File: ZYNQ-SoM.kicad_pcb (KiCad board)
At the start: 6 copper layers, 50 x 40 mm, 173 parts, among them IC501 TPS51206DSQR, J401 AXK500137YG, J402 AXK500137YG, Q201 MMBT3904, U201 xc7z010clg400, U202 W25Q256FVEI, U301 MT41K256M16TW-107_P, U501 TPS62130ARGTR, U502 TPS62130ARGTR, U503 SPX3819M5-L-3-3, U504 TPS62130ARGTR, U701 33.3333MHz

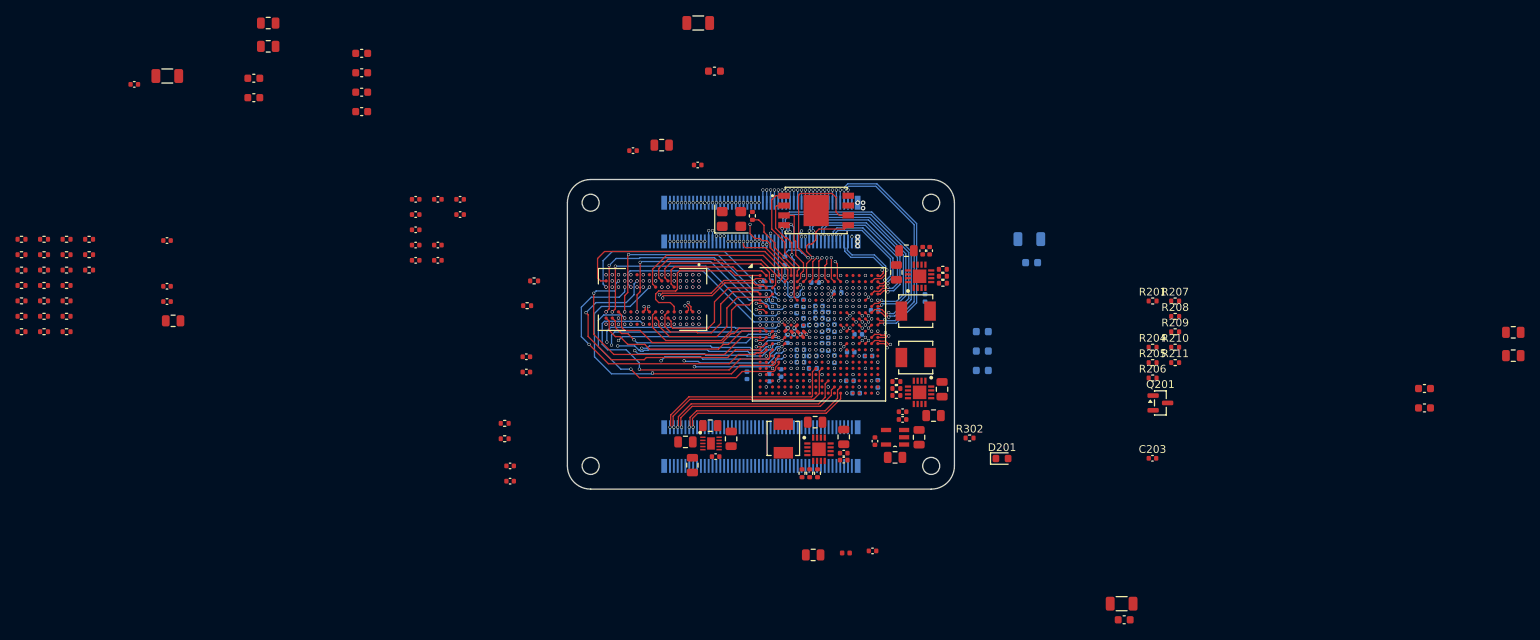
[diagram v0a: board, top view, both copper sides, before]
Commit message: layout: routing bank 34
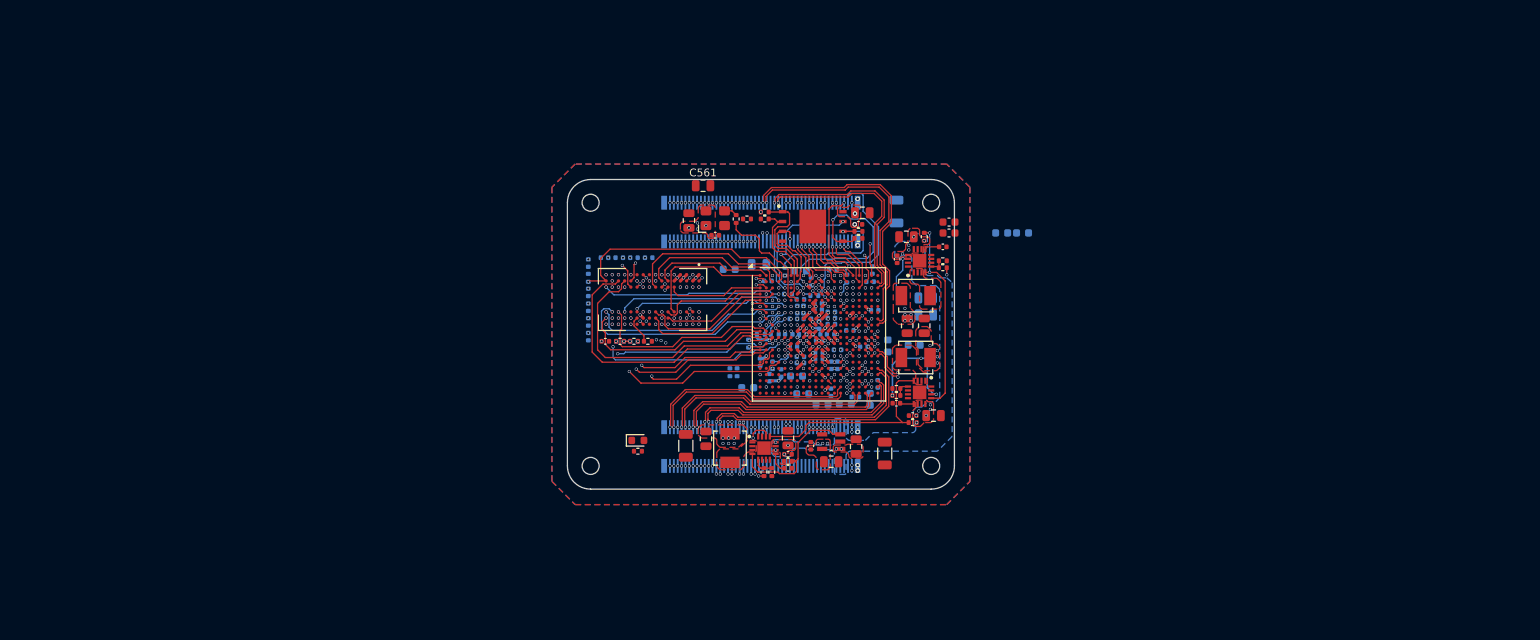
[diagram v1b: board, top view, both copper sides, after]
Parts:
- removed C315, C513, C515, C529, C531: 10u, Capacitor_SMD:C_0805_2012Metric
- removed C317, C321, C322: 100n, Capacitor_SMD:C_0402_1005Metric
- removed C518: 100u, Capacitor_SMD:C_1206_3216Metric
- removed C520, C535: 470n, Capacitor_SMD:C_0402_1005Metric
- removed IC501: TPS51206DSQR, Project:SON40P200X200X80-11N
- removed Q201: MMBT3904, Package_TO_SOT_SMD:SOT-23
- removed R204: 330R, Resistor_SMD:R_0402_1005Metric
- removed R308, R309, R310, R311, R312, R313, R314, R315, R316, R317, R318, R319, R320, R321, R322, R323, R324, R325, R326, R327, R328, R329, R330: 40R2, Resistor_SMD:R_0402_1005Metric
- added R303: 80R6, Resistor_SMD:R_0402_1005Metric, F.Cu at (108.6, 80.9)
- added R706: 10k, Resistor_SMD:R_0402_1005Metric, B.Cu at (131.5, 73.2)
- C301, C302, C303, C304, C305, C306, C308, C309, C310, C312, C313, C314, C507, C508, C521, C523, C533, C537, C546, C548, C550, C553, C557, C567, C702, FB501, R207, R211, R302, R304, R305, R306: moved to B.Cu
- C311: value 10n -> 100n; moved to B.Cu
- R201: value 1k -> 330R
- R206: value 470R -> 4k7
- R307: value 40R2 -> 80R6
- U202: footprint Project:IC_W25N04KVZEIU -> Project:SON127P800X600X80-9N-D
- moved C561 106.9 mm to (117.5, 60.8)
- moved C521 92.9 mm to (146.3, 77.5), turned to 180 degrees
- moved C525 91.7 mm to (149.3, 65.5)
- moved C567 91.6 mm to (120.9, 71.6)
- moved C527 91.5 mm to (149.3, 66.9)
- moved C523 91.0 mm to (146.3, 75.3), turned to 180 degrees
- moved C553 87.3 mm to (158.8, 66.9)
- moved C540 85.5 mm to (138.1, 64.3)
- moved C557 84.1 mm to (156.1, 66.9), turned to 180 degrees
- moved C546 82.0 mm to (130.1, 71.8)
- moved R307 78.4 mm to (106.8, 80.9)
- moved C537 75.7 mm to (135.9, 89.0), turned to 180 degrees
- moved C533 74.8 mm to (132.9, 89.1), turned to 180 degrees
- moved R205 67.5 mm to (109.1, 95.1)
- moved R209 55.0 mm to (125.5, 65.1)
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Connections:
- net Net-(U501-SW_1) renamed /POWER/1V0_SW
- net Net-(U502-SW_1) renamed /POWER/1V5_SW
- net Net-(U504-SW_1) renamed /POWER/1V8_SW
- C311 pad 1: VTTREF -> +VTTREF
- C313 pad 1: VTTREF -> +VTTREF
- C561 pad 1: +1V8 -> +3V3
- C567 pad 1: +1V8 -> +3V3
- C573 pad 1: +1V8 -> +3V3
- D201 pad 2: DONE -> +3V3
- J401 pad 100: unconnected-(J401-Pad100) -> GND
- J401 pad 15: unconnected-(J401-Pad15) -> GND
- J401 pad 16: unconnected-(J401-Pad16) -> GND
- J401 pad 18: unconnected-(J401-Pad18) -> PL_B34_IO22_P
- J401 pad 20: unconnected-(J401-Pad20) -> PL_B34_IO22_N
- J401 pad 21: unconnected-(J401-Pad21) -> GND
- J401 pad 22: unconnected-(J401-Pad22) -> GND
- J401 pad 24: unconnected-(J401-Pad24) -> PL_B34_IO12_N
- J401 pad 26: unconnected-(J401-Pad26) -> PL_B34_IO12_P
- J401 pad 27: unconnected-(J401-Pad27) -> GND
- J401 pad 28: unconnected-(J401-Pad28) -> GND
- J401 pad 30: unconnected-(J401-Pad30) -> PL_B34_IO20_P
- J401 pad 32: unconnected-(J401-Pad32) -> PL_B34_IO20_N
- J401 pad 33: unconnected-(J401-Pad33) -> GND
- J401 pad 34: unconnected-(J401-Pad34) -> GND
- J401 pad 36: unconnected-(J401-Pad36) -> PL_B34_IO13_N
- J401 pad 38: unconnected-(J401-Pad38) -> PL_B34_IO13_P
- J401 pad 39: unconnected-(J401-Pad39) -> GND
- J401 pad 40: unconnected-(J401-Pad40) -> GND
- J401 pad 42: unconnected-(J401-Pad42) -> PL_B34_IO21_N
- J401 pad 44: unconnected-(J401-Pad44) -> PL_B34_IO21_P
- J401 pad 45: unconnected-(J401-Pad45) -> GND
- J401 pad 46: unconnected-(J401-Pad46) -> GND
- J401 pad 48: unconnected-(J401-Pad48) -> PL_B34_IO24_N
- J401 pad 50: unconnected-(J401-Pad50) -> PL_B34_IO24_P
- J401 pad 51: unconnected-(J401-Pad51) -> GND
- J401 pad 52: unconnected-(J401-Pad52) -> GND
- J401 pad 54: unconnected-(J401-Pad54) -> PL_B34_IO18_P
- J401 pad 56: unconnected-(J401-Pad56) -> PL_B34_IO18_N
- J401 pad 57: unconnected-(J401-Pad57) -> GND
- J401 pad 58: unconnected-(J401-Pad58) -> GND
- J401 pad 60: unconnected-(J401-Pad60) -> PL_B34_IO10_N
- J401 pad 62: unconnected-(J401-Pad62) -> PL_B34_IO10_P
- J401 pad 63: unconnected-(J401-Pad63) -> GND
- J401 pad 64: unconnected-(J401-Pad64) -> GND
- J401 pad 66: unconnected-(J401-Pad66) -> PL_B34_IO5_N
- J401 pad 68: unconnected-(J401-Pad68) -> PL_B34_IO5_P
- J401 pad 69: unconnected-(J401-Pad69) -> GND
- J401 pad 70: unconnected-(J401-Pad70) -> GND
- J401 pad 72: unconnected-(J401-Pad72) -> PL_B34_IO15_P
- J401 pad 74: unconnected-(J401-Pad74) -> PL_B34_IO15_N
- J401 pad 75: unconnected-(J401-Pad75) -> GND
- J401 pad 76: unconnected-(J401-Pad76) -> GND
- J401 pad 78: unconnected-(J401-Pad78) -> PL_B34_IO16_P
- J401 pad 80: unconnected-(J401-Pad80) -> PL_B34_IO16_N
- J401 pad 81: unconnected-(J401-Pad81) -> GND
- J401 pad 82: unconnected-(J401-Pad82) -> GND
- J401 pad 84: unconnected-(J401-Pad84) -> PL_B34_IO17_N
- J401 pad 86: PL_B34_IO8_N -> PL_B34_IO17_P
- J401 pad 87: unconnected-(J401-Pad87) -> GND
- J401 pad 88: PL_B34_IO8_P -> GND
- J401 pad 90: unconnected-(J401-Pad90) -> PL_B34_IO7_N
- J401 pad 92: PL_B34_IO4_N -> PL_B34_IO7_P
- J401 pad 93: unconnected-(J401-Pad93) -> GND
- J401 pad 94: PL_B34_IO4_P -> GND
- J401 pad 96: PL_B34_IO1_P -> PL_B34_IO8_N
- J401 pad 98: PL_B34_IO1_N -> PL_B34_IO8_P
- J401 pad 99: unconnected-(J401-Pad99) -> GND
- J402 pad 11: PL_B35_IO1_N -> PS_MIO20
- J402 pad 12: PL_B35_IO22_P -> DONE
- J402 pad 13: PL_B35_IO1_P -> PS_MIO22
- J402 pad 14: PL_B35_IO22_N -> PS_POR_B
- J402 pad 17: PL_B35_IO4_P -> PS_MIO24
- J402 pad 18: PL_B35_IO20_P -> PS_MIO19
- J402 pad 19: PL_B35_IO4_N -> PS_MIO26
- J402 pad 20: PL_B35_IO20_N -> PS_MIO25
- J402 pad 23: PL_B35_IO15_P -> SD_DATA3
- J402 pad 24: PL_B35_IO13_P -> PS_MIO17
- J402 pad 25: PL_B35_IO15_N -> I2C0_SCL
- J402 pad 26: PL_B35_IO13_N -> PS_MIO21
- J402 pad 29: PL_B35_IO19_P -> I2C0_SDA
- J402 pad 30: PL_B35_IO14_P -> PS_MIO23
- J402 pad 31: PL_B35_IO19_N -> SD_DATA1
- J402 pad 32: PL_B35_IO14_N -> PS_MIO27
- J402 pad 35: PL_B35_IO18_P -> QSPI_D2_PS_MIO4
- J402 pad 36: PL_B35_IO16_N -> PS_MIO49
- J402 pad 37: PL_B35_IO18_N -> QSPI_D3_PS_MIO5
- J402 pad 38: PL_B35_IO16_P -> PS_MIO47
- J402 pad 42: PL_B35_IO5_N -> PL_B35_IO1_N
- J402 pad 44: PL_B35_IO5_P -> PL_B35_IO1_P
- J402 pad 47: PS_MIO47 -> PS_MIO16
- J402 pad 48: PL_B35_IO23_N -> PL_B35_IO17_N
- J402 pad 49: PS_MIO48 -> PS_MIO18
- J402 pad 5: PL_B35_IO2_P -> SD_DATA2
- J402 pad 50: PL_B35_IO23_P -> PL_B35_IO17_P
- J402 pad 53: I2C0_SDA -> PS_MIO53
- J402 pad 54: PL_B35_IO7_N -> PL_B35_IO9_N
- J402 pad 55: I2C0_SCL -> PS_MIO48
- J402 pad 56: PL_B35_IO7_P -> PL_B35_IO9_P
- J402 pad 59: PS_MIO9 -> PS_MIO52
- J402 pad 6: PL_B35_IO17_N -> SD_DATA0
- J402 pad 60: PL_B35_IO8_P -> PL_B35_IO7_N
- J402 pad 61: SD_DATA1 -> OTG_NXT
- J402 pad 62: PL_B35_IO8_N -> PL_B35_IO7_P
- J402 pad 65: SD_DATA3 -> OTG_DATA4
- J402 pad 66: PL_B35_IO9_N -> PL_B35_IO11_N
- J402 pad 67: SD_CMD -> OTG_DATA2
- J402 pad 68: PL_B35_IO9_P -> PL_B35_IO11_P
- J402 pad 7: PL_B35_IO2_N -> SD_CMD
- J402 pad 71: SD_CLK -> OTG_DATA7
- J402 pad 72: PL_B35_IO10_P -> PL_B35_IO14_P
- J402 pad 73: SD_DATA0 -> OTG_nRST
- J402 pad 74: PL_B35_IO10_N -> PL_B35_IO14_N
- J402 pad 77: SD_DATA2 -> OTG_DATA0
- J402 pad 78: PL_B35_IO3_N -> PL_B35_IO12_N
- J402 pad 79: OTG_DATA0 -> OTG_STP
- J402 pad 8: PL_B35_IO17_P -> SD_CLK
- J402 pad 80: PL_B35_IO3_P -> PL_B35_IO12_P
- J402 pad 83: OTG_DATA6 -> OTG_DATA1
- J402 pad 84: OTG_DATA7 -> PL_B35_IO13_N
- J402 pad 86: OTG_nRST -> PL_B35_IO13_P
- J402 pad 89: OTG_DATA2 -> OTG_DATA6
- J402 pad 90: OTG_NXT -> TCK
- J402 pad 91: OTG_DATA5 -> OTG_CLK
- J402 pad 92: OTG_DATA4 -> TMS
- J402 pad 95: OTG_CLK -> OTG_DATA5
- J402 pad 96: OTG_STP -> TDO
- J402 pad 98: OTG_DATA1 -> TDI
- R201 pad 1: +1V5 -> +3V3
- R201 pad 2: Net-(Q201-B) -> DONE
- R205 pad 2: Net-(Q201-C) -> GND
- R207 pad 1: +3V3 -> GND
- R307 pad 1: /DDR3/DDR_A0 -> +1V5
- R307 pad 2: +DDRVTT -> +VTTREF
- U201 pad A13: Net-(U201F-VCCO_MIO1_501[4]-PadA13) -> +3V3
- U201 pad B16: Net-(U201F-VCCO_MIO1_501[4]-PadA13) -> +3V3
- U201 pad C6: PS_MIO11 -> unconnected-(U201E-PS_MIO11_500-PadC6)
- U201 pad D12: Net-(U201F-VCCO_MIO1_501[4]-PadA13) -> +3V3
- U201 pad D9: PS_MIO12 -> unconnected-(U201E-PS_MIO12_500-PadD9)
- U201 pad E11: PS_MIO_VREF -> unconnected-(U201F-PS_MIO_VREF_501-PadE11)
- U201 pad E15: Net-(U201F-VCCO_MIO1_501[4]-PadA13) -> +3V3
- U201 pad E6: PS_MIO0 -> unconnected-(U201E-PS_MIO0_500-PadE6)
- U201 pad E9: PS_MIO10 -> unconnected-(U201E-PS_MIO10_500-PadE9)
- U201 pad H6: VTTREF -> +VTTREF
- U201 pad L2: /DDR3/DDR_CLK_N -> /DDR3/DDR_CLK_P
- U201 pad M2: /DDR3/DDR_CLK_P -> /DDR3/DDR_CLK_N
- U201 pad P6: VTTREF -> +VTTREF
- U301 pad A3: /DDR3/DDR_D10 -> /DDR3/DDR_D8
- U301 pad A7: /DDR3/DDR_D14 -> /DDR3/DDR_D13
- U301 pad B8: /DDR3/DDR_D13 -> /DDR3/DDR_D14
- U301 pad C2: /DDR3/DDR_D8 -> /DDR3/DDR_D11
- U301 pad C3: /DDR3/DDR_D12 -> /DDR3/DDR_D10
- U301 pad D7: /DDR3/DDR_D11 -> /DDR3/DDR_D12
- U301 pad E3: /DDR3/DDR_D2 -> /DDR3/DDR_D6
- U301 pad F2: /DDR3/DDR_D1 -> /DDR3/DDR_D2
- U301 pad F7: /DDR3/DDR_D5 -> /DDR3/DDR_D0
- U301 pad F8: /DDR3/DDR_D6 -> /DDR3/DDR_D5
- U301 pad G2: /DDR3/DDR_D0 -> /DDR3/DDR_D1
- U301 pad H7: /DDR3/DDR_D7 -> /DDR3/DDR_D4
- U301 pad H8: /DDR3/DDR_D4 -> /DDR3/DDR_D7
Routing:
- net PL_B35_IO23_N: track 54.1 -> 0.00 mm, vias 2 -> 0
- net PL_B35_IO23_P: track 53.2 -> 0.00 mm, vias 2 -> 0
- net PL_B35_IO22_P: track 45.5 -> 0.00 mm, vias 2 -> 0
- net PL_B35_IO8_P: track 45.4 -> 0.00 mm, vias 2 -> 0
- net +VTTREF: track 0.00 -> 45.0 mm, vias 2 -> 6
- net PL_B35_IO22_N: track 44.4 -> 0.00 mm, vias 2 -> 0
- net PL_B35_IO8_N: track 44.3 -> 0.00 mm, vias 2 -> 0
- net PL_B35_IO20_P: track 43.8 -> 0.00 mm, vias 2 -> 0
- net PL_B35_IO20_N: track 43.6 -> 0.00 mm, vias 2 -> 0
- net PL_B35_IO11_P: track 0.00 -> 42.5 mm, vias 0 -> 2
- net PL_B35_IO11_N: track 0.00 -> 42.5 mm, vias 0 -> 2
- net PL_B35_IO10_N: track 41.2 -> 0.00 mm, vias 2 -> 0
- net PL_B35_IO10_P: track 40.9 -> 0.00 mm, vias 2 -> 0
- net PL_B35_IO12_P: track 0.00 -> 38.7 mm, vias 0 -> 2
- net PL_B35_IO12_N: track 0.00 -> 38.7 mm, vias 0 -> 2
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- added copper zone on F.Cu, net +1V0
- added copper zone on In4.Cu, net +1V0
- added copper zone on F.Cu, net +1V5
- added copper zone on In4.Cu, net +1V5
- added copper zone on F.Cu, net +1V8
- added copper zone on In4.Cu, net +1V8
- added copper zone on F.Cu, net +3V3
- added copper zone on In4.Cu, net +3V3
- added copper zone on B.Cu, net +5V
- added copper zone on F.Cu, net +5V
- added copper zone on In3.Cu, net +VCCIO_34
- added copper zone on In4.Cu, net +VCCIO_34
- added copper zone on In4.Cu, net +VCCIO_35
- added copper zone on F.Cu, net /POWER/1V0_SW
- added copper zone on F.Cu, net /POWER/1V5_SW
- added copper zone on F.Cu, net /POWER/1V8_SW
- added copper zone on B.Cu, net GND
- added copper zone on F.Cu, net GND
- added copper zone on In1.Cu, net GND
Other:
- board text added: "+1V5 DDR"
- board text added: "+3V3 BANK13"
- board text added: "+3V3 MIO"
- board text added: "+VCCIO 34"
- board text added: "+VCCIO 35"
- board text added: "1V0 / 1V8 MIXED VIAS FIRST"

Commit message: layout: finish basic bank34 routing
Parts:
- moved C562 4.08 mm to (126.3, 87.8)
- moved C547 0.50 mm to (134.9, 81.5)
- moved C554 0.29 mm to (134.0, 87.2)
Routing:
- net PL_B34_IO24_N: track 21.0 -> 0.69 mm
- net PL_B34_IO24_P: track 20.1 -> 0.13 mm
- net PL_B34_IO19_P: track 0.00 -> 15.2 mm, vias 0 -> 1
- net PL_B34_IO19_N: track 0.00 -> 14.8 mm, vias 0 -> 1
- net PL_B34_IO25: track 0.00 -> 9.06 mm, vias 0 -> 1
- net PL_B34_IO23_N: track 0.00 -> 8.63 mm, vias 0 -> 1
- net PL_B34_IO0: track 0.00 -> 7.80 mm, vias 0 -> 1
- net PL_B34_IO9_P: track 0.00 -> 6.77 mm
- net PL_B34_IO11_N: track 0.00 -> 6.42 mm
- net PL_B34_IO2_P: track 0.00 -> 6.38 mm, vias 0 -> 1
- net PL_B34_IO9_N: track 0.57 -> 6.77 mm
- net PL_B34_IO11_P: track 0.57 -> 6.09 mm
- net PL_B34_IO2_N: track 0.00 -> 5.45 mm, vias 0 -> 1
- net PL_B34_IO3_P: track 0.00 -> 5.36 mm
- net PL_B34_IO1_P: track 0.57 -> 5.90 mm
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- added copper zone on In3.Cu, net +1V0
- added copper zone on In3.Cu, net +1V8
- added copper zone on In3.Cu, net +3V3
- removed copper zone on In3.Cu, net +VCCIO_34

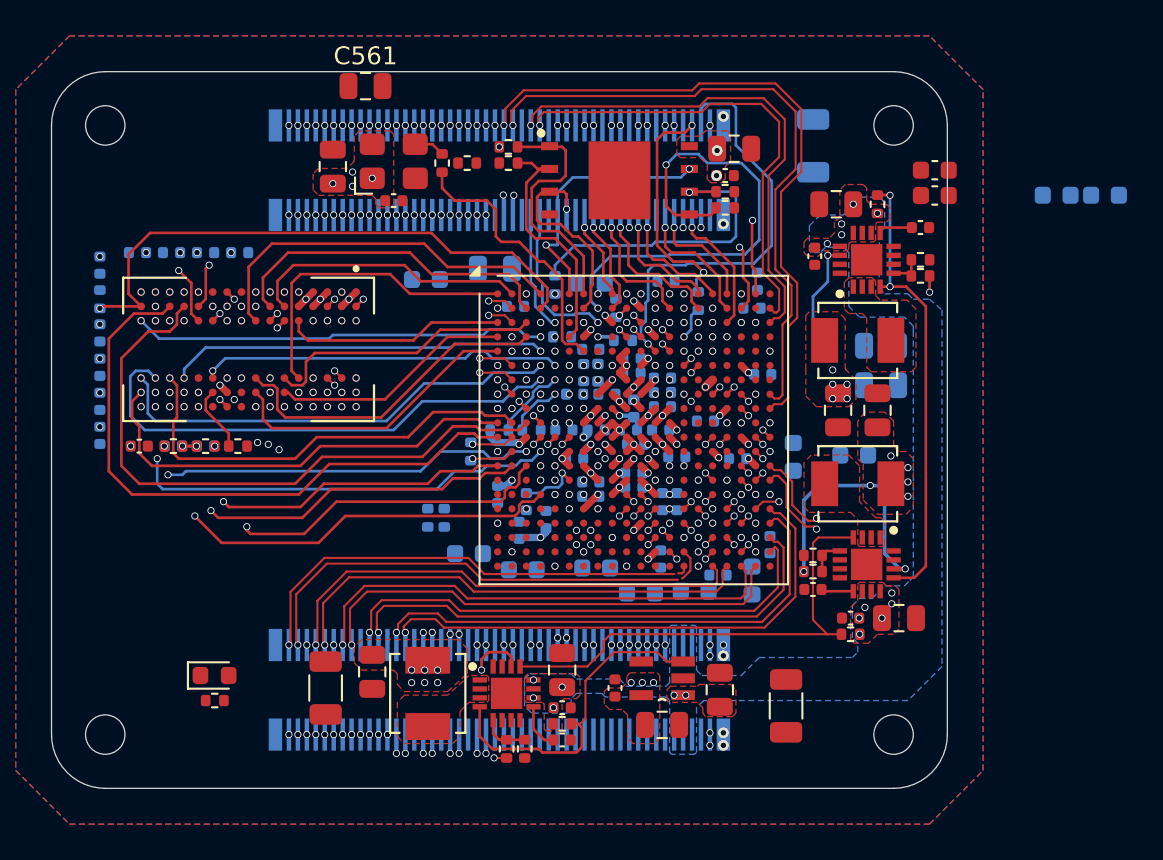
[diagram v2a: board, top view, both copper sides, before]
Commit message: layout: before rerouting ddr
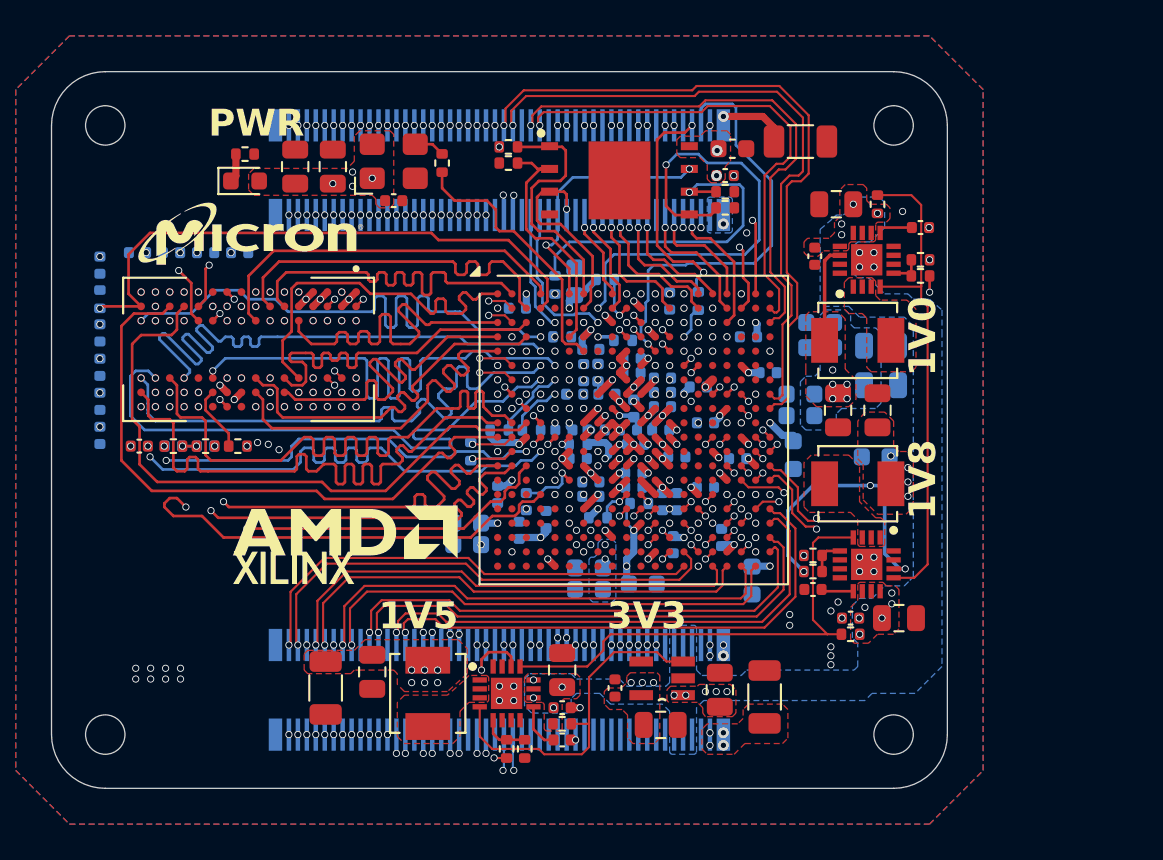
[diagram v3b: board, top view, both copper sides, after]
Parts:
- removed C537, C557: 4u7, Capacitor_SMD:C_0603_1608Metric
- C507, C540: footprint Capacitor_SMD:C_0805_2012Metric -> Capacitor_SMD:C_0603_1608Metric
- C525, C527, R201: moved to B.Cu
- C544: moved to F.Cu
- moved R205 30.5 mm to (110.8, 64.6)
- moved D201 27.7 mm to (110.8, 66.1)
- moved R201 21.3 mm to (132.8, 84.1)
- moved C567 20.9 mm to (133.0, 88.6)
- moved C553 17.4 mm to (142.9, 74.0), turned to 180 degrees
- moved C533 17.0 mm to (142.9, 75.4)
- moved C507 15.5 mm to (123.2, 86.4)
- moved C525 14.6 mm to (141.8, 78.0), turned to 180 degrees
- moved C527 14.4 mm to (141.8, 79.2), turned to 180 degrees
- moved R203 9.35 mm to (129.4, 80.8), turned to 180 degrees
- moved R202 8.58 mm to (130.5, 84.9), turned to 0 degrees
- moved C565 6.76 mm to (136.1, 77.6), turned to 0 degrees
- moved C561 5.97 mm to (113.6, 65.3), turned to 90 degrees
- moved C554 4.72 mm to (136.5, 83.2), turned to 0 degrees
- moved C562 3.86 mm to (130.0, 88.9)
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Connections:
- J401 pad 36: PL_B34_IO13_N -> PL_B34_IO13_P
- J401 pad 38: PL_B34_IO13_P -> PL_B34_IO13_N
- J401 pad 47: unconnected-(J401-Pad47) -> PL_B34_IO23_N
- J401 pad 48: PL_B34_IO24_N -> PL_B34_IO19_N
- J401 pad 49: unconnected-(J401-Pad49) -> PL_B34_IO25
- J401 pad 50: PL_B34_IO24_P -> PL_B34_IO19_P
- J401 pad 53: unconnected-(J401-Pad53) -> PL_B34_IO0
- J401 pad 55: unconnected-(J401-Pad55) -> PL_B34_IO23_P
- J401 pad 59: unconnected-(J401-Pad59) -> PL_B34_IO4_P
- J401 pad 60: PL_B34_IO10_N -> PL_B34_IO10_P
- J401 pad 61: unconnected-(J401-Pad61) -> PL_B34_IO4_N
- J401 pad 62: PL_B34_IO10_P -> PL_B34_IO10_N
- J401 pad 65: unconnected-(J401-Pad65) -> PL_B34_IO14_P
- J401 pad 67: unconnected-(J401-Pad67) -> PL_B34_IO14_N
- J401 pad 71: unconnected-(J401-Pad71) -> PL_B34_IO9_N
- J401 pad 73: unconnected-(J401-Pad73) -> PL_B34_IO9_P
- J401 pad 77: unconnected-(J401-Pad77) -> PL_B34_IO11_P
- J401 pad 79: unconnected-(J401-Pad79) -> PL_B34_IO11_N
- J401 pad 83: unconnected-(J401-Pad83) -> PL_B34_IO3_N
- J401 pad 85: unconnected-(J401-Pad85) -> PL_B34_IO3_P
- J401 pad 89: unconnected-(J401-Pad89) -> PL_B34_IO2_N
- J401 pad 91: unconnected-(J401-Pad91) -> PL_B34_IO2_P
- J401 pad 95: unconnected-(J401-Pad95) -> PL_B34_IO1_P
- J401 pad 96: PL_B34_IO8_N -> PL_B34_IO8_P
- J401 pad 97: unconnected-(J401-Pad97) -> PL_B34_IO1_N
- J401 pad 98: PL_B34_IO8_P -> PL_B34_IO8_N
- U201 pad A20: PL_B35_IO2_N -> unconnected-(U201D-IO_L2N_T0_AD8N_35-PadA20)
- U201 pad B19: PL_B35_IO2_P -> unconnected-(U201D-IO_L2P_T0_AD8P_35-PadB19)
- U201 pad B5: PS_MIO9 -> unconnected-(U201E-PS_MIO9_500-PadB5)
- U201 pad D18: PL_B35_IO3_N -> unconnected-(U201D-IO_L3N_T0_DQS_AD1N_35-PadD18)
- U201 pad D19: PL_B35_IO4_P -> unconnected-(U201D-IO_L4P_T0_35-PadD19)
- U201 pad D20: PL_B35_IO4_N -> unconnected-(U201D-IO_L4N_T0_35-PadD20)
- U201 pad E17: PL_B35_IO3_P -> unconnected-(U201D-IO_L3P_T0_DQS_AD1P_35-PadE17)
- U201 pad E18: PL_B35_IO5_P -> unconnected-(U201D-IO_L5P_T0_AD9P_35-PadE18)
- U201 pad E19: PL_B35_IO5_N -> unconnected-(U201D-IO_L5N_T0_AD9N_35-PadE19)
- U201 pad E8: PS_MIO13 -> unconnected-(U201E-PS_MIO13_500-PadE8)
- U201 pad F16: PL_B35_IO6_P -> unconnected-(U201D-IO_L6P_T0_35-PadF16)
- U201 pad F17: PL_B35_IO6_N -> unconnected-(U201D-IO_L6N_T0_VREF_35-PadF17)
- U201 pad F19: PL_B35_IO15_P -> unconnected-(U201D-IO_L15P_T2_DQS_AD12P_35-PadF19)
- U201 pad F20: PL_B35_IO15_N -> unconnected-(U201D-IO_L15N_T2_DQS_AD12N_35-PadF20)
- U201 pad G14: PL_B35_IO0 -> unconnected-(U201D-IO_0_35-PadG14)
- U201 pad G15: PL_B35_IO19_N -> unconnected-(U201D-IO_L19N_T3_VREF_35-PadG15)
- U201 pad G17: PL_B35_IO16_P -> unconnected-(U201D-IO_L16P_T2_35-PadG17)
- U201 pad G18: PL_B35_IO16_N -> unconnected-(U201D-IO_L16N_T2_35-PadG18)
- U201 pad G19: PL_B35_IO18_P -> unconnected-(U201D-IO_L18P_T2_AD13P_35-PadG19)
- U201 pad G20: PL_B35_IO18_N -> unconnected-(U201D-IO_L18N_T2_AD13N_35-PadG20)
- U201 pad H15: PL_B35_IO19_P -> unconnected-(U201D-IO_L19P_T3_35-PadH15)
- U201 pad J14: PL_B35_IO20_N -> unconnected-(U201D-IO_L20N_T3_AD6N_35-PadJ14)
- U201 pad J15: PL_B35_IO25 -> unconnected-(U201D-IO_25_35-PadJ15)
- U201 pad J16: PL_B35_IO24_N -> unconnected-(U201D-IO_L24N_T3_AD15N_35-PadJ16)
- U201 pad J19: PL_B35_IO10_N -> unconnected-(U201D-IO_L10N_T1_AD11N_35-PadJ19)
- U201 pad K14: PL_B35_IO20_P -> unconnected-(U201D-IO_L20P_T3_AD6P_35-PadK14)
- U201 pad K16: PL_B35_IO24_P -> unconnected-(U201D-IO_L24P_T3_AD15P_35-PadK16)
- U201 pad K19: PL_B35_IO10_P -> unconnected-(U201D-IO_L10P_T1_AD11P_35-PadK19)
- U201 pad L14: PL_B35_IO22_P -> unconnected-(U201D-IO_L22P_T3_AD7P_35-PadL14)
- U201 pad L15: PL_B35_IO22_N -> unconnected-(U201D-IO_L22N_T3_AD7N_35-PadL15)
- U201 pad M14: PL_B35_IO23_P -> unconnected-(U201D-IO_L23P_T3_35-PadM14)
- U201 pad M15: PL_B35_IO23_N -> unconnected-(U201D-IO_L23N_T3_35-PadM15)
- U201 pad M17: PL_B35_IO8_P -> unconnected-(U201D-IO_L8P_T1_AD10P_35-PadM17)
- U201 pad M18: PL_B35_IO8_N -> unconnected-(U201D-IO_L8N_T1_AD10N_35-PadM18)
- U201 pad N15: PL_B35_IO21_P -> unconnected-(U201D-IO_L21P_T3_DQS_AD14P_35-PadN15)
- U201 pad N16: PL_B35_IO21_N -> unconnected-(U201D-IO_L21N_T3_DQS_AD14N_35-PadN16)
- U201 pad P14: PL_B34_IO6_P -> unconnected-(U201C-IO_L6P_T0_34-PadP14)
- U201 pad P15: PL_B34_IO24_P -> unconnected-(U201C-IO_L24P_T3_34-PadP15)
- U201 pad P16: PL_B34_IO24_N -> unconnected-(U201C-IO_L24N_T3_34-PadP16)
- U201 pad R14: PL_B34_IO6_N -> unconnected-(U201C-IO_L6N_T0_VREF_34-PadR14)
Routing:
- net PL_B34_IO23_P: track 0.00 -> 42.2 mm, vias 0 -> 2
- net PL_B34_IO14_P: track 4.69 -> 41.8 mm, vias 1 -> 2
- net PL_B34_IO14_N: track 4.69 -> 41.2 mm, vias 1 -> 2
- net PL_B34_IO9_N: track 6.77 -> 42.6 mm, vias 1 -> 2
- net PL_B34_IO9_P: track 6.77 -> 42.4 mm, vias 1 -> 2
- net PL_B34_IO11_N: track 6.42 -> 39.7 mm, vias 1 -> 2
- net PL_B34_IO11_P: track 6.09 -> 39.3 mm, vias 1 -> 2
- net PL_B34_IO3_P: track 5.36 -> 38.5 mm, vias 1 -> 2
- net PL_B34_IO3_N: track 4.67 -> 37.8 mm, vias 1 -> 2
- net PL_B34_IO4_P: track 4.17 -> 36.3 mm, vias 1 -> 2
- net PL_B34_IO2_N: track 5.45 -> 36.5 mm, vias 1 -> 2
- net PL_B34_IO2_P: track 6.38 -> 37.4 mm, vias 1 -> 2
- net PL_B34_IO1_P: track 5.90 -> 36.3 mm, vias 1 -> 2
- net PL_B34_IO1_N: track 5.70 -> 36.1 mm, vias 1 -> 2
- net PL_B34_IO4_N: track 3.85 -> 32.2 mm, vias 1 -> 2
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- added copper zone on B.Cu, net +1V0
- added copper zone on In2.Cu, net +1V5
- added copper zone on B.Cu, net +1V8
- added copper zone on F.Cu, net +VCCIO_34
- added copper zone on B.Cu, net +VCCIO_35
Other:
- board text added: "1V0"
- board text added: "1V5"
- board text added: "1V8"
- board text added: "3V3"
- board text added: "PWR"
